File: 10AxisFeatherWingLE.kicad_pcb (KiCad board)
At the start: 2 copper layers, 50.8 x 22.9 mm, 23 parts, among them J1 feather long, J2 feather short, J3 grove connector, J4 feather long, J5 feather short, J6 feather breakout, U1 LSM9DS1, U2 BMP280

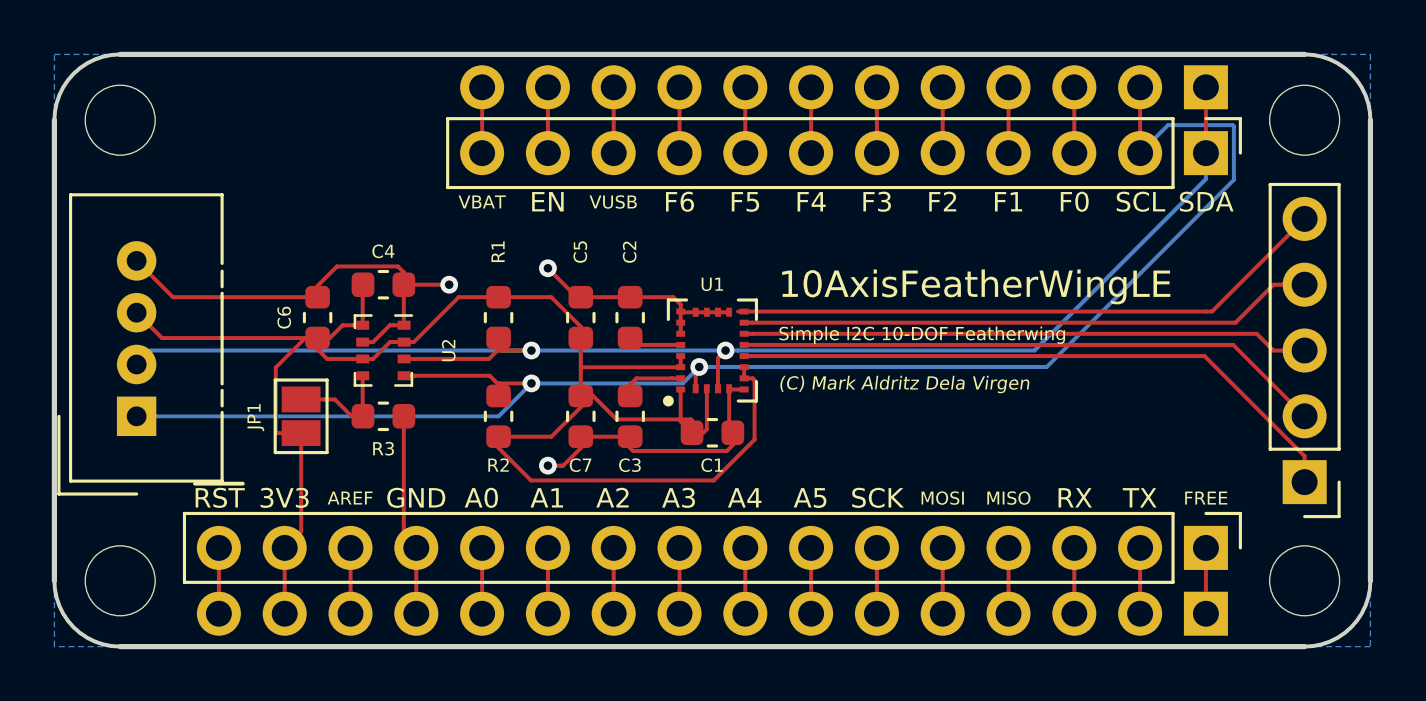
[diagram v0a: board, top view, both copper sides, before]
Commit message: Corrected capacitor values
CAP and C1 capacitors were flipped, fixed
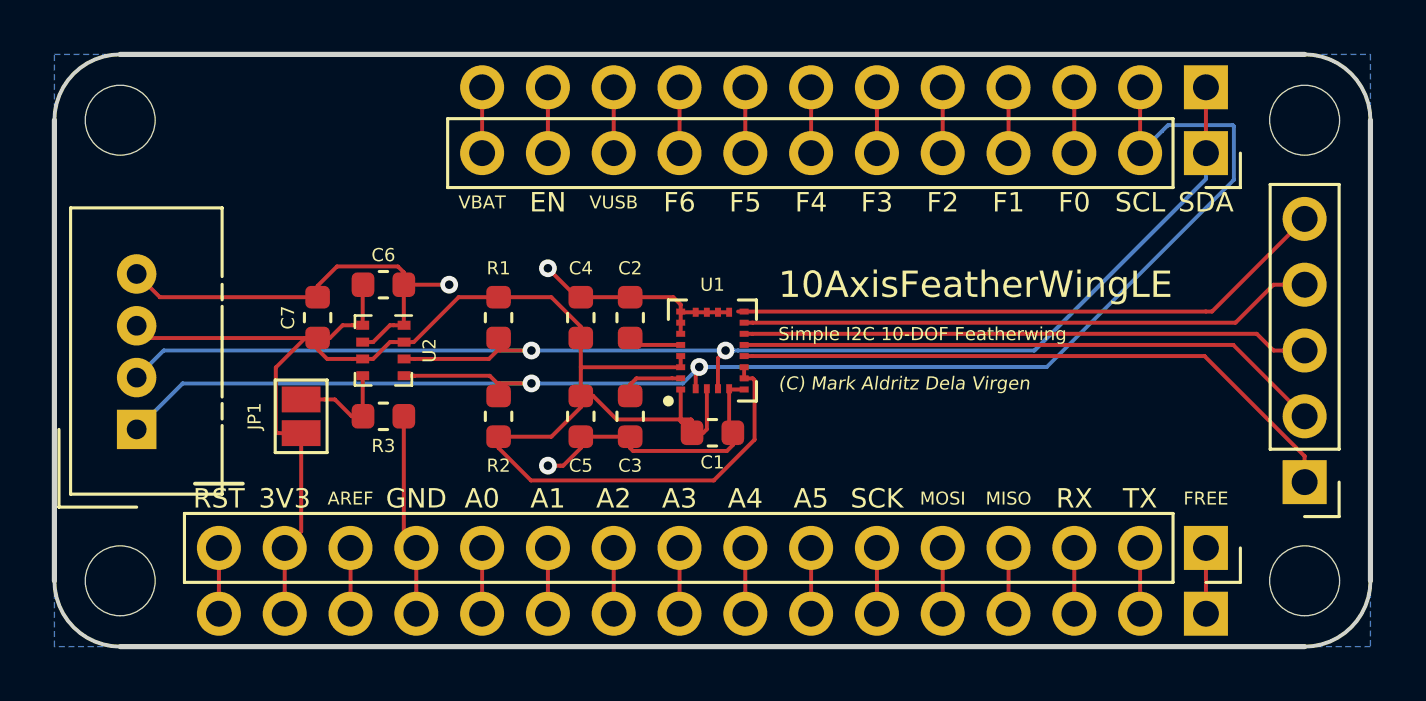
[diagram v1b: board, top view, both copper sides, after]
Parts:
- C2: value 100nF -> 10nF
- C3: value 10nF -> 100nF
- J3: renamed from J4; footprint Connector_PinHeader_2.54mm:PinHeader_1x16_P2.54mm_Vertical -> Connector_PinSocket_2.54mm:PinSocket_1x16_P2.54mm_Vertical
- J4: renamed from J5; footprint Connector_PinHeader_2.54mm:PinHeader_1x12_P2.54mm_Vertical -> Connector_PinSocket_2.54mm:PinSocket_1x12_P2.54mm_Vertical
- moved J5 0.51 mm to (28.6, 39.9)
- renumbered C5 to C4, C7 to C5, C4 to C6, C6 to C7, J3 to J5

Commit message: Minor format fix
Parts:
- removed REF** (x4): MountingHole_2.7mm_M2.5, MountingHole:MountingHole_2.7mm_M2.5
- added H1: MountingHole, MountingHole:MountingHole_2.7mm_M2.5, F.Cu at (27.9, 27.9)
- added H2: MountingHole, MountingHole:MountingHole_2.7mm_M2.5, F.Cu at (27.9, 45.7)
- added H3: MountingHole, MountingHole:MountingHole_2.7mm_M2.5, F.Cu at (73.7, 27.9)
- added H4: MountingHole, MountingHole:MountingHole_2.7mm_M2.5, F.Cu at (73.7, 45.7)
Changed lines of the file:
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@@
     (add_net "Net-(C3-Pad2)")
   )
-  (module Connector_PinSocket_2.54mm:PinSocket_1x12_P2.54mm_Vertical (layer F.Cu)
+  (module MountingHole:MountingHole_2.7mm_M2.5 locked (layer F.Cu)
+    (at 73.66 45.72)
+    (descr "Mounting Hole 2.7mm, no annular, M2.5")
+    (tags "mounting hole 2.7mm no annular m2.5")
+    (attr virtual)
+    (fp_text reference H4 (at 0 -3.7) (layer F.SilkS) hide
+      (effects (font (size 1 1) (thickness 0.15)))
+    )
+    (fp_text value MountingHole (at 0 3.7) (layer F.Fab) hide
+      (effects (font (size 1 1) (thickness 0.15)))
+    )
+    (fp_circle (center 0 0) (end 2.95 0) (layer F.CrtYd) (width 0.05))
+    (fp_circle (center 0 0) (end 2.7 0) (layer Cmts.User) (width 0.15))
+    (fp_text user %R (at 0.3 0) (layer F.Fab)
+      (effects (font (size 1 1) (thickness 0.15)))
+    )
+    (pad 1 np_thru_hole circle (at 0 0) (size 2.7 2.7) (drill 2.7) (layers *.Cu *.Mask))
+  )
+  (module MountingHole:MountingHole_2.7mm_M2.5 locked (layer F.Cu)
+    (at 73.66 27.94)
+    (descr "Mounting Hole 2.7mm, no annular, M2.5")
+    (tags "mounting hole 2.7mm no annular m2.5")
+    (attr virtual)
+    (fp_text reference H3 (at 0 -3.7) (layer F.SilkS) hide
+      (effects (font (size 1 1) (thickness 0.15)))
+    )
+    (fp_text value MountingHole (at 0 3.7) (layer F.Fab) hide
+      (effects (font (size 1 1) (thickness 0.15)))
+    )
+    (fp_circle (center 0 0) (end 2.95 0) (layer F.CrtYd) (width 0.05))
+    (fp_circle (center 0 0) (end 2.7 0) (layer Cmts.User) (width 0.15))
+    (fp_text user %R (at 0.3 0) (layer F.Fab)
+      (effects (font (size 1 1) (thickness 0.15)))
+    )
+    (pad 1 np_thru_hole circle (at 0 0) (size 2.7 2.7) (drill 2.7) (layers *.Cu *.Mask))
+  )
+  (module MountingHole:MountingHole_2.7mm_M2.5 locked (layer F.Cu)
+    (at 27.94 45.72)
+    (descr "Mounting Hole 2.7mm, no annular, M2.5")
+    (tags "mounting hole 2.7mm no annular m2.5")
+    (attr virtual)
+    (fp_text reference H2 (at 0 -3.7) (layer F.SilkS) hide
+      (effects (font (size 1 1) (thickness 0.15)))
+    )
+    (fp_text value MountingHole (at 0 3.7) (layer F.Fab) hide
+      (effects (font (size 1 1) (thickness 0.15)))
+    )
+    (fp_circle (center 0 0) (end 2.95 0) (layer F.CrtYd) (width 0.05))
+    (fp_circle (center 0 0) (end 2.7 0) (layer Cmts.User) (width 0.15))
+    (fp_text user %R (at 0.3 0) (layer F.Fab)
+      (effects (font (size 1 1) (thickness 0.15)))
+    )
+    (pad 1 np_thru_hole circle (at 0 0) (size 2.7 2.7) (drill 2.7) (layers *.Cu *.Mask))
+  )
+  (module MountingHole:MountingHole_2.7mm_M2.5 locked (layer F.Cu)
+    (at 27.94 27.94)
+    (descr "Mounting Hole 2.7mm, no annular, M2.5")
+    (tags "mounting hole 2.7mm no annular m2.5")
+    (attr virtual)
+    (fp_text reference H1 (at 0 -3.7) (layer F.SilkS) hide
+      (effects (font (size 1 1) (thickness 0.15)))
+    )
+    (fp_text value MountingHole (at 0 3.7) (layer F.Fab) hide
+      (effects (font (size 1 1) (thickness 0.15)))
+    )
+    (fp_circle (center 0 0) (end 2.95 0) (layer F.CrtYd) (width 0.05))
+    (fp_circle (center 0 0) (end 2.7 0) (layer Cmts.User) (width 0.15))
+    (fp_text user %R (at 0.3 0) (layer F.Fab)
+      (effects (font (size 1 1) (thickness 0.15)))
+    )
+    (pad 1 np_thru_hole circle (at 0 0) (size 2.7 2.7) (drill 2.7) (layers *.Cu *.Mask))
+  )
+  (module Connector_PinSocket_2.54mm:PinSocket_1x12_P2.54mm_Vertical locked (layer F.Cu)
     (at 69.85 29.21 270)
     (descr "Through hole straight socket strip, 1x12, 2.54mm pitch, single row (from Kicad 4.0.7), script generated")
@@
     )
   )
-  (module Connector_PinSocket_2.54mm:PinSocket_1x16_P2.54mm_Vertical (layer F.Cu)
+  (module Connector_PinSocket_2.54mm:PinSocket_1x16_P2.54mm_Vertical locked (layer F.Cu)
     (at 69.85 44.45 270)
     (descr "Through hole straight socket strip, 1x16, 2.54mm pitch, single row (from Kicad 4.0.7), script generated")
@@
     )
   )
-  (module MountingHole:MountingHole_2.7mm_M2.5 locked (layer F.Cu)
-    (at 73.66 27.94)
-    (descr "Mounting Hole 2.7mm, no annular, M2.5")
-    (tags "mounting hole 2.7mm no annular m2.5")
-    (attr virtual)
-    (fp_text reference REF** (at 0 -3.7) (layer F.SilkS) hide
-      (effects (font (size 1 1) (thickness 0.15)))
-    )
-    (fp_text value MountingHole_2.7mm_M2.5 (at 0 3.7) (layer F.Fab) hide
-      (effects (font (size 1 1) (thickness 0.15)))
-    )
-    (fp_text user %R (at 0.3 0) (layer F.Fab) hide
-      (effects (font (size 1 1) (thickness 0.15)))
-    )
-    (fp_circle (center 0 0) (end 2.7 0) (layer Cmts.User) (width 0.15))
-    (fp_circle (center 0 0) (end 2.95 0) (layer F.CrtYd) (width 0.05))
-    (pad 1 np_thru_hole circle (at 0 0) (size 2.7 2.7) (drill 2.7) (layers *.Cu *.Mask))
-  )
-  (module MountingHole:MountingHole_2.7mm_M2.5 locked (layer F.Cu)
-    (at 73.66 45.72)
-    (descr "Mounting Hole 2.7mm, no annular, M2.5")
-    (tags "mounting hole 2.7mm no annular m2.5")
-    (attr virtual)
-    (fp_text reference REF** (at 0 -3.7) (layer F.SilkS) hide
-      (effects (font (size 1 1) (thickness 0.15)))
-    )
-    (fp_text value MountingHole_2.7mm_M2.5 (at 0 3.7) (layer F.Fab) hide
-      (effects (font (size 1 1) (thickness 0.15)))
-    )
-    (fp_circle (center 0 0) (end 2.95 0) (layer F.CrtYd) (width 0.05))
-    (fp_circle (center 0 0) (end 2.7 0) (layer Cmts.User) (width 0.15))
-    (fp_text user %R (at 0.3 0) (layer F.Fab) hide
-      (effects (font (size 1 1) (thickness 0.15)))
-    )
-    (pad 1 np_thru_hole circle (at 0 0) (size 2.7 2.7) (drill 2.7) (layers *.Cu *.Mask))
-  )
-  (module MountingHole:MountingHole_2.7mm_M2.5 locked (layer F.Cu)
-    (at 27.94 45.72)
-    (descr "Mounting Hole 2.7mm, no annular, M2.5")
-    (tags "mounting hole 2.7mm no annular m2.5")
-    (attr virtual)
-    (fp_text reference REF** (at 0 -3.7) (layer F.SilkS) hide
-      (effects (font (size 1 1) (thickness 0.15)))
-    )
-    (fp_text value MountingHole_2.7mm_M2.5 (at 0 3.7) (layer F.Fab) hide
-      (effects (font (size 1 1) (thickness 0.15)))
-    )
-    (fp_text user %R (at 0.3 0) (layer F.Fab) hide
-      (effects (font (size 1 1) (thickness 0.15)))
-    )
-    (fp_circle (center 0 0) (end 2.7 0) (layer Cmts.User) (width 0.15))
-    (fp_circle (center 0 0) (end 2.95 0) (layer F.CrtYd) (width 0.05))
-    (pad 1 np_thru_hole circle (at 0 0) (size 2.7 2.7) (drill 2.7) (layers *.Cu *.Mask))
-  )
-  (module MountingHole:MountingHole_2.7mm_M2.5 locked (layer F.Cu)
-    (at 27.94 27.94)
-    (descr "Mounting Hole 2.7mm, no annular, M2.5")
-    (tags "mounting hole 2.7mm no annular m2.5")
-    (attr virtual)
-    (fp_text reference REF** (at 0 -3.7) (layer F.SilkS) hide
-      (effects (font (size 1 1) (thickness 0.15)))
-    )
-    (fp_text value MountingHole_2.7mm_M2.5 (at 0 3.7) (layer F.Fab) hide
-      (effects (font (size 1 1) (thickness 0.15)))
-    )
-    (fp_circle (center 0 0) (end 2.95 0) (layer F.CrtYd) (width 0.05))
-    (fp_circle (center 0 0) (end 2.7 0) (layer Cmts.User) (width 0.15))
-    (fp_text user %R (at 0.3 0) (layer F.Fab) hide
-      (effects (font (size 1 1) (thickness 0.15)))
-    )
-    (pad 1 np_thru_hole circle (at 0 0) (size 2.7 2.7) (drill 2.7) (layers *.Cu *.Mask))
-  )
-  (module Connector_PinHeader_2.54mm:PinHeader_1x16_P2.54mm_Vertical (layer B.Cu)
+  (module Connector_PinHeader_2.54mm:PinHeader_1x16_P2.54mm_Vertical locked (layer B.Cu)
     (at 69.85 46.99 90)
     (descr "Through hole straight pin header, 1x16, 2.54mm pitch, single row")
@@
     )
   )
-  (module Connector_PinHeader_2.54mm:PinHeader_1x12_P2.54mm_Vertical (layer B.Cu)
+  (module Connector_PinHeader_2.54mm:PinHeader_1x12_P2.54mm_Vertical locked (layer B.Cu)
     (at 69.85 26.67 90)
     (descr "Through hole straight pin header, 1x12, 2.54mm pitch, single row")

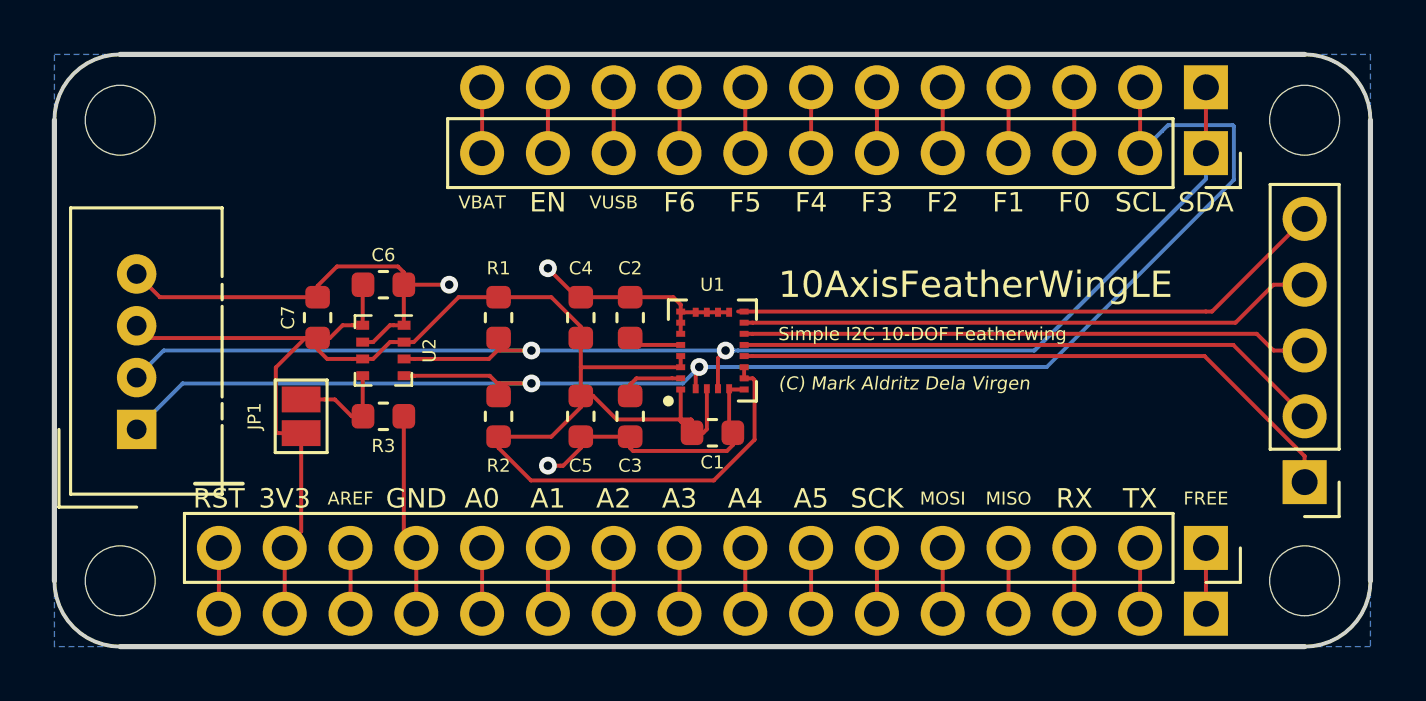
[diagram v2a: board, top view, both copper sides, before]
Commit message: Increased trace width
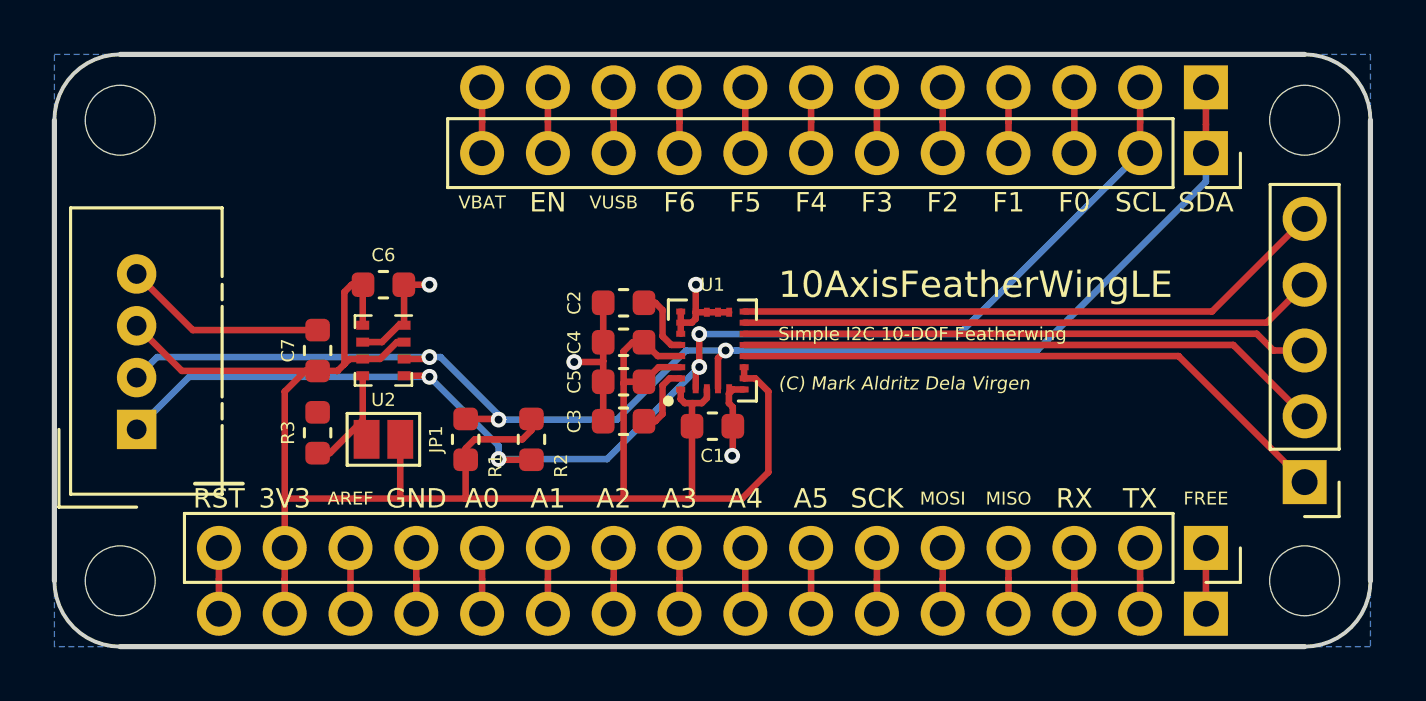
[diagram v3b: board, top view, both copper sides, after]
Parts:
- moved R1 4.87 mm to (41.3, 40.3), turned to 90 degrees
- moved JP1 3.30 mm to (38.1, 40.3), turned to 180 degrees
- moved R3 2.62 mm to (35.6, 40.0), turned to 270 degrees
- moved C5 2.12 mm to (47.4, 38.0), turned to 180 degrees
- moved C4 1.91 mm to (47.4, 36.5), turned to 180 degrees
- moved R2 1.55 mm to (43.8, 40.3), turned to 270 degrees
- moved C7 1.27 mm to (35.6, 36.8)
- moved C2 0.63 mm to (47.4, 35.0), turned to 180 degrees
- moved C3 0.32 mm to (47.4, 39.6), turned to 0 degrees
- moved C1 0.25 mm to (50.8, 39.8)
- renumbered J6 to J5, J5 to J6
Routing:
- net GND: track 45.0 -> 27.8 mm, vias 3 -> 4
- net /SCL: track 61.4 -> 52.5 mm, vias 2 -> 4
- net +3V3: track 70.6 -> 74.5 mm
- net /SDA: track 55.1 -> 54.0 mm, vias 2 -> 3
- net Net-(C2-Pad1): track 2.06 -> 2.68 mm
- net /DRDY: track 24.2 -> 23.7 mm
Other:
- net class Default: trace_width 0.1524 -> 0.254; via_dia 0.6858 -> 0.6096; via_drill 0.3302 -> 0.3048

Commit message: Changed grove connector to STEMMA
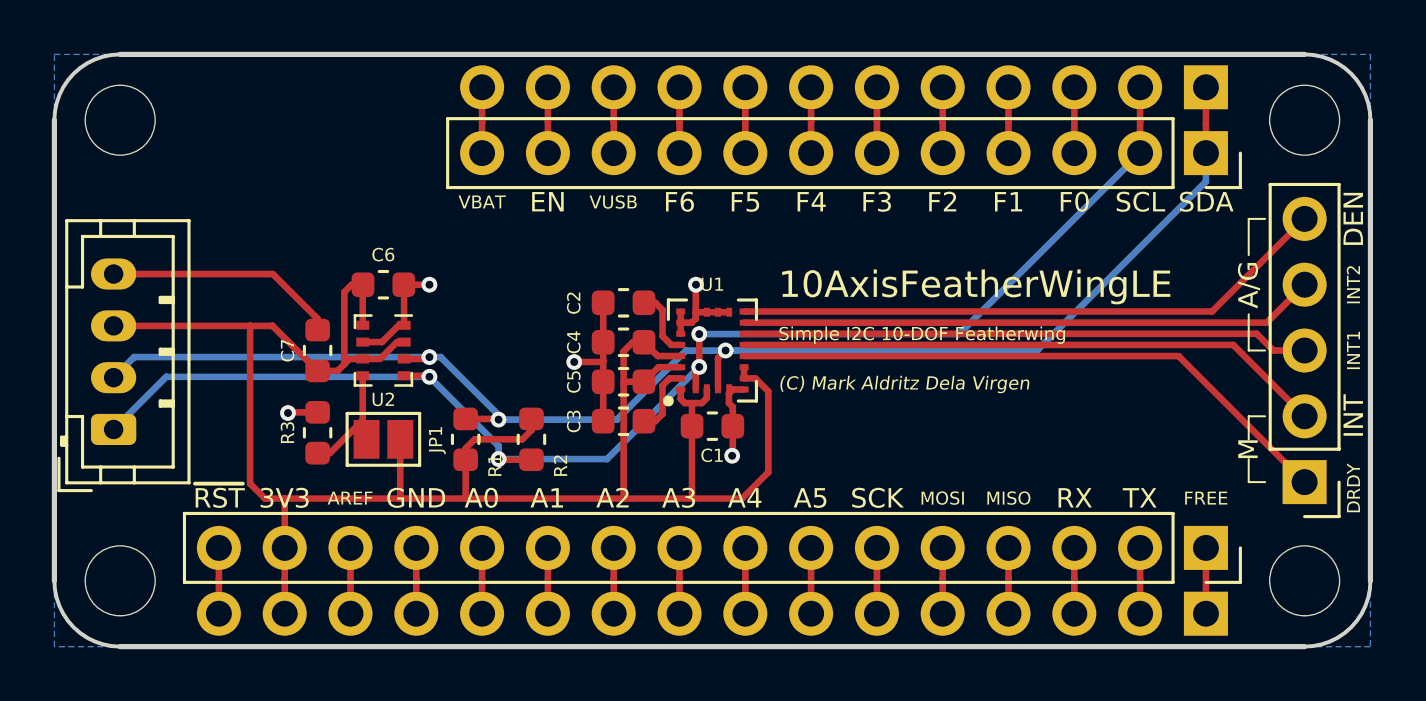
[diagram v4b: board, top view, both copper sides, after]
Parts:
- J6: value grove connector -> stemma connector; footprint Connector:NS-Tech_Grove_1x04_P2mm_Vertical -> Connector_JST:JST_PH_B4B-PH-K_1x04_P2.00mm_Vertical
- moved J6 0.89 mm to (27.7, 39.9), turned to 90 degrees
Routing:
- net +3V3: track 74.5 -> 77.3 mm
- net GND: track 27.8 -> 30.1 mm, vias 4 -> 5
- net /SCL: track 52.5 -> 53.4 mm
- net /SDA: track 54.0 -> 54.9 mm
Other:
- board text added: "A/G"
- board text added: "DEN"
- board text added: "DRDY"
- board text added: "INT"
- board text added: "INT1"
- board text added: "INT2"
- board text added: "M"
